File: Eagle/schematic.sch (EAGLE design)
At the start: 3 parts, among them IC1 ATMEGA328-20P

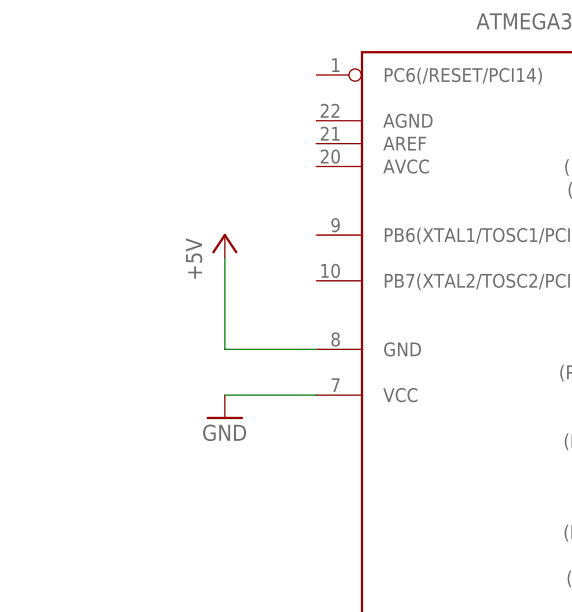
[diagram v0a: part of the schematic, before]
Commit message: Add crystal to schematic.
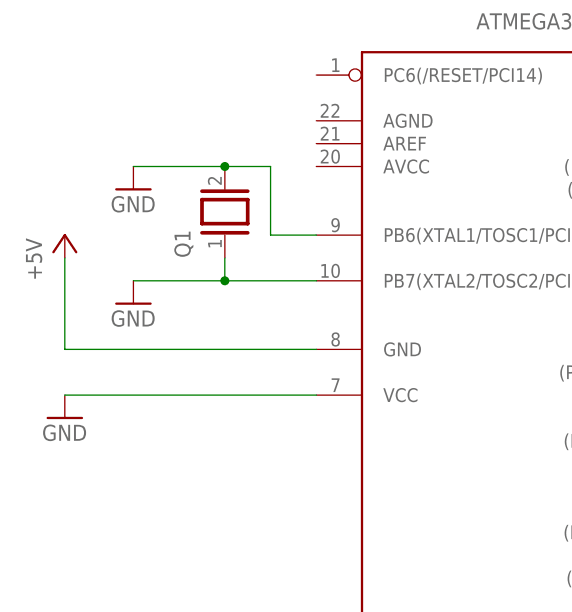
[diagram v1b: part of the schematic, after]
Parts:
- added Q1: (no value), special:XTAL
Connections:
- net GND: now also IC1.PB6(XTAL1/TOSC1/PCI6), IC1.PB7(XTAL2/TOSC2/PCI7), Q1.1, Q1.2
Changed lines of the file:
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@@
 <part name="GND2" library="supply1" library_urn="urn:adsk.eagle:library:371" deviceset="GND" device=""/>
 <part name="R1" library="piher" library_urn="urn:adsk.eagle:library:324" deviceset="PC16S" device=""/>
+<part name="Q1" library="special" library_urn="urn:adsk.eagle:library:367" deviceset="XTAL" device=""/>
+<part name="GND3" library="supply1" library_urn="urn:adsk.eagle:library:371" deviceset="GND" device=""/>
+<part name="GND4" library="supply1" library_urn="urn:adsk.eagle:library:371" deviceset="GND" device=""/>
 </parts>
 <sheets>
@@
 <instance part="IC1" gate="G$1" x="63.5" y="55.88"/>
 <instance part="DIS1" gate="G$1" x="134.62" y="104.14"/>
-<instance part="GND1" gate="1" x="30.48" y="45.72"/>
-<instance part="P+1" gate="1" x="30.48" y="66.04"/>
+<instance part="GND1" gate="1" x="12.7" y="45.72"/>
+<instance part="P+1" gate="1" x="12.7" y="66.04"/>
 <instance part="P+2" gate="1" x="111.76" y="88.9"/>
 <instance part="GND2" gate="1" x="106.68" y="81.28"/>
 <instance part="R1" gate="G$1" x="109.22" y="73.66"/>
+<instance part="Q1" gate="G$1" x="30.48" y="68.58" rot="R90"/>
+<instance part="GND3" gate="1" x="20.32" y="58.42"/>
+<instance part="GND4" gate="1" x="20.32" y="71.12"/>
 </instances>
 <busses>
@@
 <segment>
 <pinref part="IC1" gate="G$1" pin="VCC"/>
-<wire x1="40.64" y1="48.26" x2="30.48" y2="48.26" width="0.1524" layer="91"/>
+<wire x1="40.64" y1="48.26" x2="12.7" y2="48.26" width="0.1524" layer="91"/>
 <pinref part="GND1" gate="1" pin="GND"/>
 </segment>
@@
 <wire x1="104.14" y1="66.04" x2="104.14" y2="68.58" width="0.1524" layer="91"/>
 </segment>
+<segment>
+<pinref part="IC1" gate="G$1" pin="PB6(XTAL1/TOSC1/PCI6)"/>
+<wire x1="40.64" y1="66.04" x2="35.56" y2="66.04" width="0.1524" layer="91"/>
+<wire x1="35.56" y1="66.04" x2="35.56" y2="73.66" width="0.1524" layer="91"/>
+<pinref part="Q1" gate="G$1" pin="2"/>
+<wire x1="35.56" y1="73.66" x2="30.48" y2="73.66" width="0.1524" layer="91"/>
+<junction x="30.48" y="73.66"/>
+<pinref part="GND4" gate="1" pin="GND"/>
+<wire x1="30.48" y1="73.66" x2="20.32" y2="73.66" width="0.1524" layer="91"/>
+</segment>
+<segment>
+<pinref part="IC1" gate="G$1" pin="PB7(XTAL2/TOSC2/PCI7)"/>
+<pinref part="Q1" gate="G$1" pin="1"/>
+<wire x1="40.64" y1="60.96" x2="30.48" y2="60.96" width="0.1524" layer="91"/>
+<wire x1="30.48" y1="60.96" x2="30.48" y2="63.5" width="0.1524" layer="91"/>
+<pinref part="GND3" gate="1" pin="GND"/>
+<wire x1="20.32" y1="60.96" x2="30.48" y2="60.96" width="0.1524" layer="91"/>
+<junction x="30.48" y="60.96"/>
+</segment>
 </net>
 <net name="+5V" class="0">
 <segment>
 <pinref part="IC1" gate="G$1" pin="GND"/>
-<wire x1="40.64" y1="53.34" x2="30.48" y2="53.34" width="0.1524" layer="91"/>
-<wire x1="30.48" y1="53.34" x2="30.48" y2="63.5" width="0.1524" layer="91"/>
+<wire x1="40.64" y1="53.34" x2="12.7" y2="53.34" width="0.1524" layer="91"/>
+<wire x1="12.7" y1="53.34" x2="12.7" y2="63.5" width="0.1524" layer="91"/>
 <pinref part="P+1" gate="1" pin="+5V"/>
 </segment>
